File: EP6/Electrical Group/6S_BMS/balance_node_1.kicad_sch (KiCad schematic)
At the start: 8 parts, among them Q4 SI2301CDS-T1-GE3

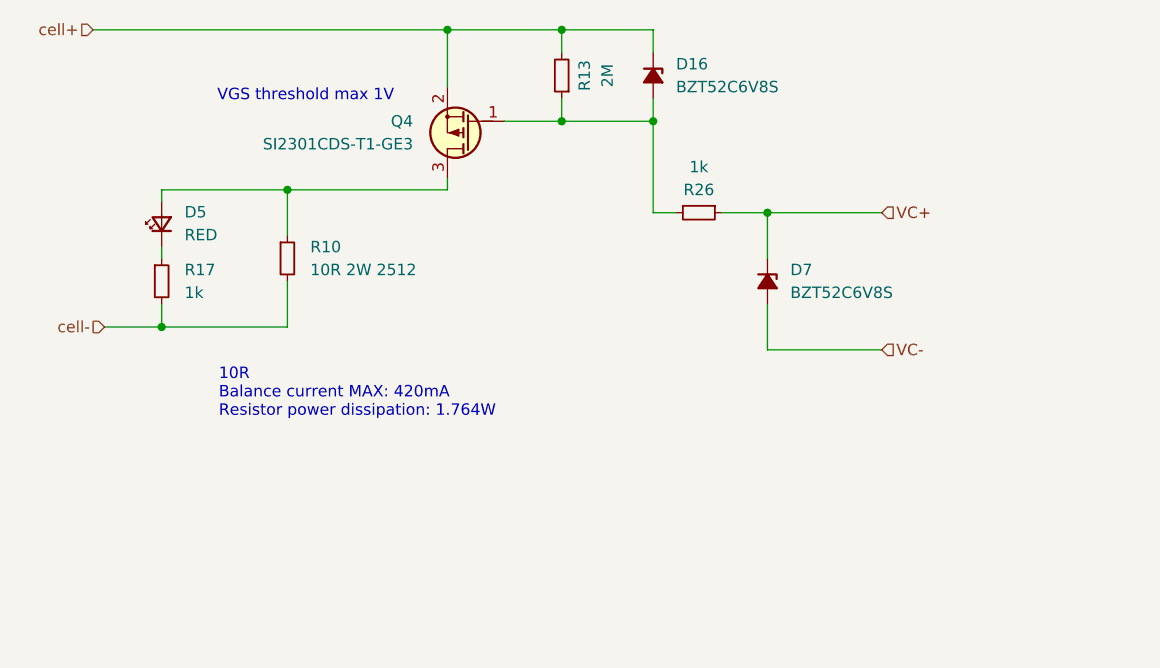
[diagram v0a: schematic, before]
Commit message: 6S BMS sch cleanup
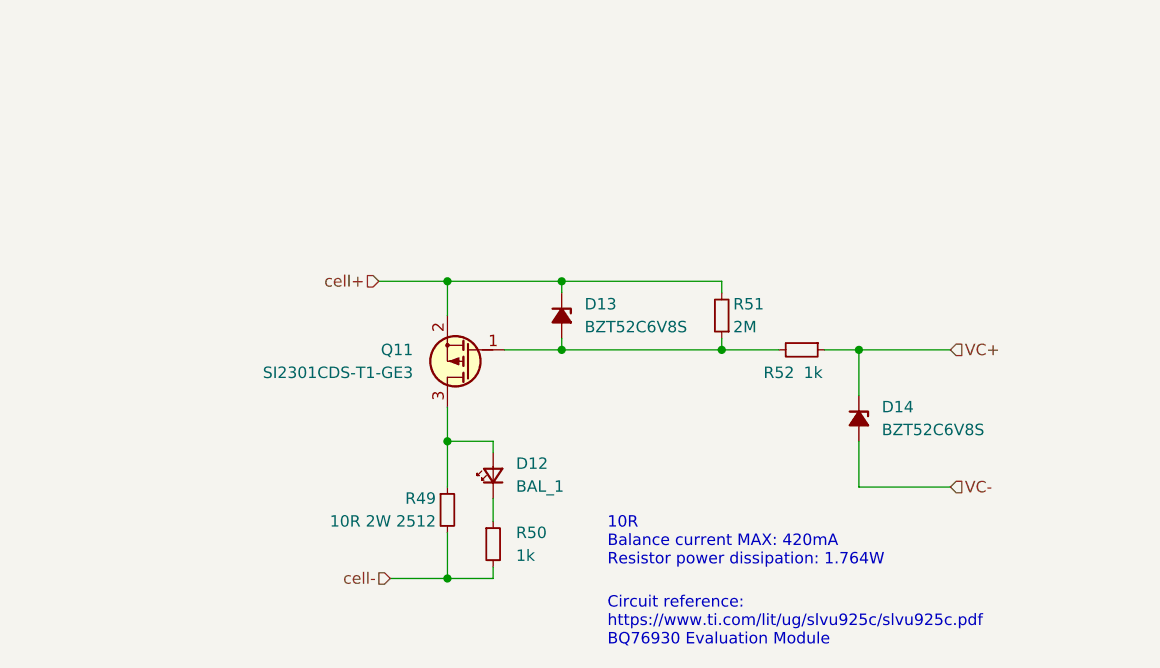
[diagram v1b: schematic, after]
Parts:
- removed D16, D7: BZT52C6V8S, Diode_SMD:D_SOD-323, symbol Device:D_Zener_Small_Filled
- removed D5: RED, LED_SMD:LED_0603_1608Metric, symbol Device:LED_Small
- removed Q4: SI2301CDS-T1-GE3, Package_TO_SOT_SMD:SOT-23, symbol PCM_Transistor_MOSFET_AKL:Q_PMOS-E_Generic_GSD
- removed R10: 10R 2W 2512, Resistor_SMD:R_2512_6332Metric, symbol Device:R_Small
- removed R13: 2M, Resistor_SMD:R_0402_1005Metric, symbol Device:R_Small
- removed R17, R26: 1k, Resistor_SMD:R_0402_1005Metric, symbol Device:R_Small
- added D12: BAL_1, LED_SMD:LED_0603_1608Metric, symbol Device:LED_Small
- added D13, D14: BZT52C6V8S, Diode_SMD:D_SOD-323, symbol Device:D_Zener_Small_Filled
- added Q11: SI2301CDS-T1-GE3, Package_TO_SOT_SMD:SOT-23, symbol PCM_Transistor_MOSFET_AKL:Q_PMOS-E_Generic_GSD
- added R49: 10R 2W 2512, Resistor_SMD:R_2512_6332Metric, symbol Device:R_Small
- added R50, R52: 1k, Resistor_SMD:R_0402_1005Metric, symbol Device:R_Small
- added R51: 2M, Resistor_SMD:R_0402_1005Metric, symbol Device:R_Small
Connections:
- net VC+: now also D14.1 (K), R52.1
- net VC-: now also D14.2 (A)
- net cell+: now also D13.1 (K), Q11.2 (S), R51.2
- net cell-: now also R49.2, R50.2
- new net: D13.2 (A), Q11.1 (G), R51.1, R52.2
- new net: D12.2 (A), Q11.3 (D), R49.1
- new net: D12.1 (K), R50.1
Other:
- note added: "Circuit reference: https://www.ti.com/lit/ug/slvu925c/slvu925c.pdf BQ76930 Evaluation Module"
- note removed: "VGS threshold max 1V"

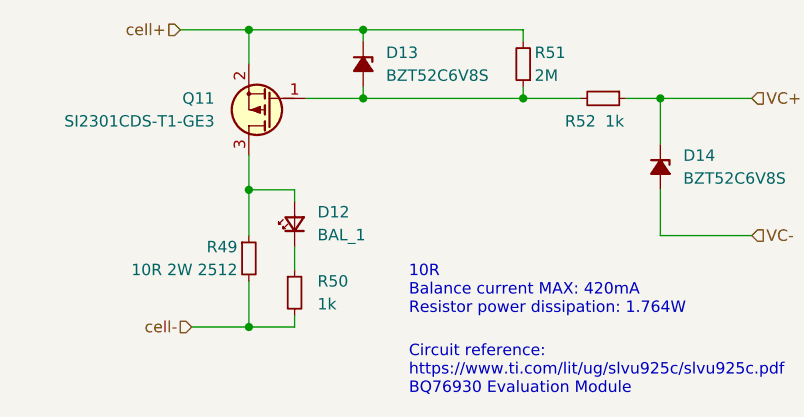
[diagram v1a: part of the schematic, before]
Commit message: fix net ties
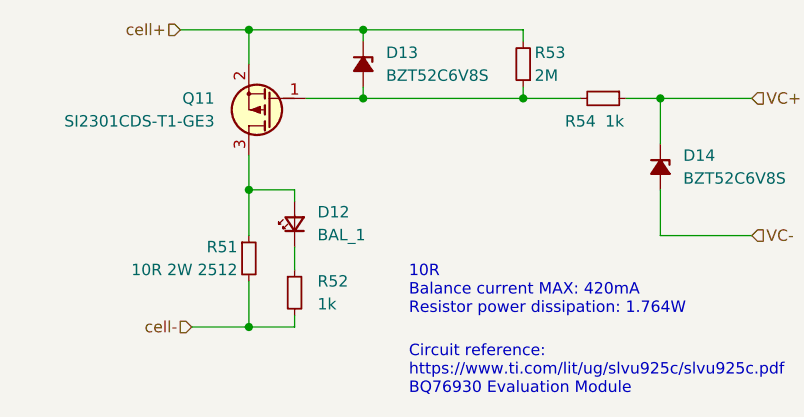
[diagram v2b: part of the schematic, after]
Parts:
- renumbered R49 to R51, R50 to R52, R51 to R53, R52 to R54
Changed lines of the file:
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@@
 		(on_board yes)
 		(dnp no)
-		(property "Reference" "R49"
+		(property "Reference" "R51"
 			(at 127 107.95 0)
 			(effects
@@
 			(project "6S_BMS"
 				(path "/0942010f-46b1-4fe9-9f5e-a3ebd22b3e41/52dfc651-89b8-4cbc-8d60-c4ae9fe4057d"
-					(reference "R49")
-					(unit 1)
-				)
-				(path "/0942010f-46b1-4fe9-9f5e-a3ebd22b3e41/8cdfc8a8-e74f-4198-87ef-7f931d327daa"
-					(reference "R45")
-					(unit 1)
-				)
-				(path "/0942010f-46b1-4fe9-9f5e-a3ebd22b3e41/92fdac40-2976-4651-87ac-086c10e148fd"
-					(reference "R61")
-					(unit 1)
-				)
-				(path "/0942010f-46b1-4fe9-9f5e-a3ebd22b3e41/d0b81097-a7cf-4d08-9411-1236a5f1861b"
-					(reference "R53")
-					(unit 1)
-				)
-				(path "/0942010f-46b1-4fe9-9f5e-a3ebd22b3e41/d47f883f-ac19-4acb-9090-d30d2c19de6d"
-					(reference "R65")
-					(unit 1)
-				)
-				(path "/0942010f-46b1-4fe9-9f5e-a3ebd22b3e41/f57ef34a-2774-492f-8a82-625e3b6c6734"
-					(reference "R57")
+					(reference "R51")
+					(unit 1)
+				)
+				(path "/0942010f-46b1-4fe9-9f5e-a3ebd22b3e41/8cdfc8a8-e74f-4198-87ef-7f931d327daa"
+					(reference "R47")
+					(unit 1)
+				)
+				(path "/0942010f-46b1-4fe9-9f5e-a3ebd22b3e41/92fdac40-2976-4651-87ac-086c10e148fd"
+					(reference "R63")
+					(unit 1)
+				)
+				(path "/0942010f-46b1-4fe9-9f5e-a3ebd22b3e41/d0b81097-a7cf-4d08-9411-1236a5f1861b"
+					(reference "R55")
+					(unit 1)
+				)
+				(path "/0942010f-46b1-4fe9-9f5e-a3ebd22b3e41/d47f883f-ac19-4acb-9090-d30d2c19de6d"
+					(reference "R67")
+					(unit 1)
+				)
+				(path "/0942010f-46b1-4fe9-9f5e-a3ebd22b3e41/f57ef34a-2774-492f-8a82-625e3b6c6734"
+					(reference "R59")
 					(unit 1)
 				)
@@
 		(dnp no)
 		(fields_autoplaced yes)
-		(property "Reference" "R50"
+		(property "Reference" "R52"
 			(at 135.89 111.76 0)
 			(effects
@@
 			(project "6S_BMS"
 				(path "/0942010f-46b1-4fe9-9f5e-a3ebd22b3e41/52dfc651-89b8-4cbc-8d60-c4ae9fe4057d"
-					(reference "R50")
-					(unit 1)
-				)
-				(path "/0942010f-46b1-4fe9-9f5e-a3ebd22b3e41/8cdfc8a8-e74f-4198-87ef-7f931d327daa"
-					(reference "R46")
-					(unit 1)
-				)
-				(path "/0942010f-46b1-4fe9-9f5e-a3ebd22b3e41/92fdac40-2976-4651-87ac-086c10e148fd"
-					(reference "R62")
-					(unit 1)
-				)
-				(path "/0942010f-46b1-4fe9-9f5e-a3ebd22b3e41/d0b81097-a7cf-4d08-9411-1236a5f1861b"
-					(reference "R54")
-					(unit 1)
-				)
-				(path "/0942010f-46b1-4fe9-9f5e-a3ebd22b3e41/d47f883f-ac19-4acb-9090-d30d2c19de6d"
-					(reference "R66")
-					(unit 1)
-				)
-				(path "/0942010f-46b1-4fe9-9f5e-a3ebd22b3e41/f57ef34a-2774-492f-8a82-625e3b6c6734"
-					(reference "R58")
+					(reference "R52")
+					(unit 1)
+				)
+				(path "/0942010f-46b1-4fe9-9f5e-a3ebd22b3e41/8cdfc8a8-e74f-4198-87ef-7f931d327daa"
+					(reference "R48")
+					(unit 1)
+				)
+				(path "/0942010f-46b1-4fe9-9f5e-a3ebd22b3e41/92fdac40-2976-4651-87ac-086c10e148fd"
+					(reference "R64")
+					(unit 1)
+				)
+				(path "/0942010f-46b1-4fe9-9f5e-a3ebd22b3e41/d0b81097-a7cf-4d08-9411-1236a5f1861b"
+					(reference "R56")
+					(unit 1)
+				)
+				(path "/0942010f-46b1-4fe9-9f5e-a3ebd22b3e41/d47f883f-ac19-4acb-9090-d30d2c19de6d"
+					(reference "R68")
+					(unit 1)
+				)
+				(path "/0942010f-46b1-4fe9-9f5e-a3ebd22b3e41/f57ef34a-2774-492f-8a82-625e3b6c6734"
+					(reference "R60")
 					(unit 1)
 				)
@@
 		(on_board yes)
 		(dnp no)
-		(property "Reference" "R51"
+		(property "Reference" "R53"
 			(at 160.02 86.36 0)
 			(effects
@@
 			(project "6S_BMS"
 				(path "/0942010f-46b1-4fe9-9f5e-a3ebd22b3e41/52dfc651-89b8-4cbc-8d60-c4ae9fe4057d"
-					(reference "R51")
-					(unit 1)
-				)
-				(path "/0942010f-46b1-4fe9-9f5e-a3ebd22b3e41/8cdfc8a8-e74f-4198-87ef-7f931d327daa"
-					(reference "R47")
-					(unit 1)
-				)
-				(path "/0942010f-46b1-4fe9-9f5e-a3ebd22b3e41/92fdac40-2976-4651-87ac-086c10e148fd"
-					(reference "R63")
-					(unit 1)
-				)
-				(path "/0942010f-46b1-4fe9-9f5e-a3ebd22b3e41/d0b81097-a7cf-4d08-9411-1236a5f1861b"
-					(reference "R55")
-					(unit 1)
-				)
-				(path "/0942010f-46b1-4fe9-9f5e-a3ebd22b3e41/d47f883f-ac19-4acb-9090-d30d2c19de6d"
-					(reference "R67")
-					(unit 1)
-				)
-				(path "/0942010f-46b1-4fe9-9f5e-a3ebd22b3e41/f57ef34a-2774-492f-8a82-625e3b6c6734"
-					(reference "R59")
+					(reference "R53")
+					(unit 1)
+				)
+				(path "/0942010f-46b1-4fe9-9f5e-a3ebd22b3e41/8cdfc8a8-e74f-4198-87ef-7f931d327daa"
+					(reference "R49")
+					(unit 1)
+				)
+				(path "/0942010f-46b1-4fe9-9f5e-a3ebd22b3e41/92fdac40-2976-4651-87ac-086c10e148fd"
+					(reference "R65")
+					(unit 1)
+				)
+				(path "/0942010f-46b1-4fe9-9f5e-a3ebd22b3e41/d0b81097-a7cf-4d08-9411-1236a5f1861b"
+					(reference "R57")
+					(unit 1)
+				)
+				(path "/0942010f-46b1-4fe9-9f5e-a3ebd22b3e41/d47f883f-ac19-4acb-9090-d30d2c19de6d"
+					(reference "R69")
+					(unit 1)
+				)
+				(path "/0942010f-46b1-4fe9-9f5e-a3ebd22b3e41/f57ef34a-2774-492f-8a82-625e3b6c6734"
+					(reference "R61")
 					(unit 1)
 				)
@@
 		(on_board yes)
 		(dnp no)
-		(property "Reference" "R52"
+		(property "Reference" "R54"
 			(at 165.1 93.98 90)
 			(effects
@@
 			(project "6S_BMS"
 				(path "/0942010f-46b1-4fe9-9f5e-a3ebd22b3e41/52dfc651-89b8-4cbc-8d60-c4ae9fe4057d"
-					(reference "R52")
-					(unit 1)
-				)
-				(path "/0942010f-46b1-4fe9-9f5e-a3ebd22b3e41/8cdfc8a8-e74f-4198-87ef-7f931d327daa"
-					(reference "R48")
-					(unit 1)
-				)
-				(path "/0942010f-46b1-4fe9-9f5e-a3ebd22b3e41/92fdac40-2976-4651-87ac-086c10e148fd"
-					(reference "R64")
-					(unit 1)
-				)
-				(path "/0942010f-46b1-4fe9-9f5e-a3ebd22b3e41/d0b81097-a7cf-4d08-9411-1236a5f1861b"
-					(reference "R56")
-					(unit 1)
-				)
-				(path "/0942010f-46b1-4fe9-9f5e-a3ebd22b3e41/d47f883f-ac19-4acb-9090-d30d2c19de6d"
-					(reference "R68")
-					(unit 1)
-				)
-				(path "/0942010f-46b1-4fe9-9f5e-a3ebd22b3e41/f57ef34a-2774-492f-8a82-625e3b6c6734"
-					(reference "R60")
-					(unit 1)
-				)
+					(reference "R54")
+					(unit 1)
+				)
+				(path "/0942010f-46b1-4fe9-9f5e-a3ebd22b3e41/8cdfc8a8-e74f-4198-87ef-7f931d327daa"
+					(reference "R50")
+					(unit 1)
+				)
+				(path "/0942010f-46b1-4fe9-9f5e-a3ebd22b3e41/92fdac40-2976-4651-87ac-086c10e148fd"
+					(reference "R66")
+					(unit 1)
+				)
+				(path "/0942010f-46b1-4fe9-9f5e-a3ebd22b3e41/d0b81097-a7cf-4d08-9411-1236a5f1861b"
+					(reference "R58")
+					(unit 1)
+				)
+				(path "/0942010f-46b1-4fe9-9f5e-a3ebd22b3e41/d47f883f-ac19-4acb-9090-d30d2c19de6d"
+					(reference "R70")
+					(unit 1)
+				)
+				(path "/0942010f-46b1-4fe9-9f5e-a3ebd22b3e41/f57ef34a-2774-492f-8a82-625e3b6c6734"
+					(reference "R62")
+					(unit 1)
+				)

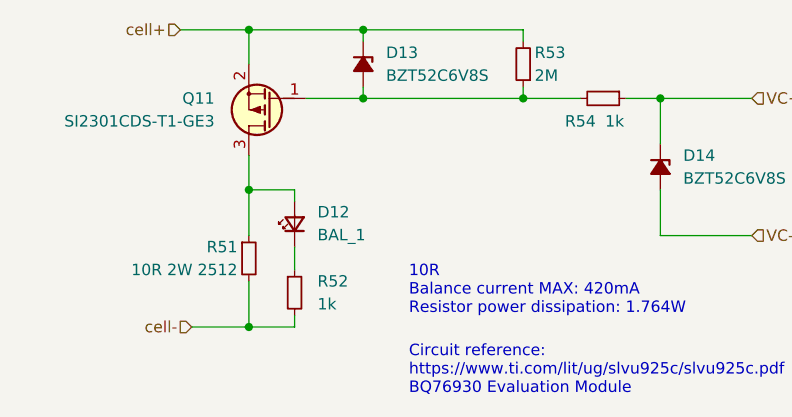
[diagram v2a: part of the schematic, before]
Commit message: front panel board connectors
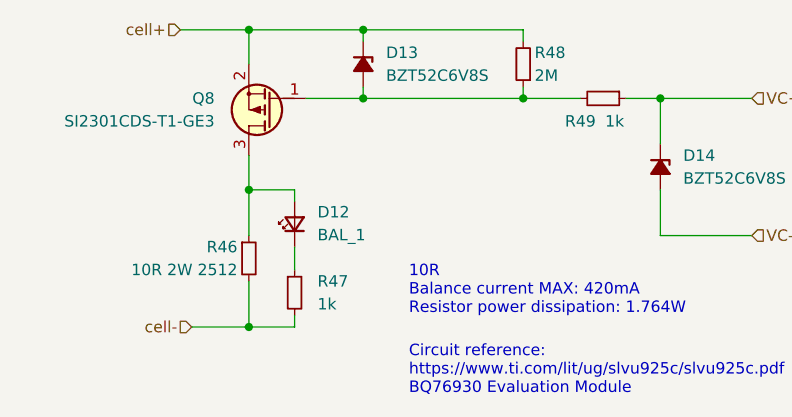
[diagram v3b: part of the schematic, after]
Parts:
- renumbered Q11 to Q8, R51 to R46, R52 to R47, R53 to R48, R54 to R49
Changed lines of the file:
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@@
 		(on_board yes)
 		(dnp no)
-		(property "Reference" "Q11"
+		(property "Reference" "Q8"
 			(at 124.46 91.44 0)
 			(effects
@@
 			(project "6S_BMS"
 				(path "/0942010f-46b1-4fe9-9f5e-a3ebd22b3e41/52dfc651-89b8-4cbc-8d60-c4ae9fe4057d"
+					(reference "Q8")
+					(unit 1)
+				)
+				(path "/0942010f-46b1-4fe9-9f5e-a3ebd22b3e41/8cdfc8a8-e74f-4198-87ef-7f931d327daa"
+					(reference "Q7")
+					(unit 1)
+				)
+				(path "/0942010f-46b1-4fe9-9f5e-a3ebd22b3e41/92fdac40-2976-4651-87ac-086c10e148fd"
 					(reference "Q11")
 					(unit 1)
 				)
-				(path "/0942010f-46b1-4fe9-9f5e-a3ebd22b3e41/8cdfc8a8-e74f-4198-87ef-7f931d327daa"
+				(path "/0942010f-46b1-4fe9-9f5e-a3ebd22b3e41/d0b81097-a7cf-4d08-9411-1236a5f1861b"
+					(reference "Q9")
+					(unit 1)
+				)
+				(path "/0942010f-46b1-4fe9-9f5e-a3ebd22b3e41/d47f883f-ac19-4acb-9090-d30d2c19de6d"
+					(reference "Q12")
+					(unit 1)
+				)
+				(path "/0942010f-46b1-4fe9-9f5e-a3ebd22b3e41/f57ef34a-2774-492f-8a82-625e3b6c6734"
 					(reference "Q10")
-					(unit 1)
-				)
-				(path "/0942010f-46b1-4fe9-9f5e-a3ebd22b3e41/92fdac40-2976-4651-87ac-086c10e148fd"
-					(reference "Q14")
-					(unit 1)
-				)
-				(path "/0942010f-46b1-4fe9-9f5e-a3ebd22b3e41/d0b81097-a7cf-4d08-9411-1236a5f1861b"
-					(reference "Q12")
-					(unit 1)
-				)
-				(path "/0942010f-46b1-4fe9-9f5e-a3ebd22b3e41/d47f883f-ac19-4acb-9090-d30d2c19de6d"
-					(reference "Q15")
-					(unit 1)
-				)
-				(path "/0942010f-46b1-4fe9-9f5e-a3ebd22b3e41/f57ef34a-2774-492f-8a82-625e3b6c6734"
-					(reference "Q13")
 					(unit 1)
 				)
@@
 		(on_board yes)
 		(dnp no)
-		(property "Reference" "R51"
+		(property "Reference" "R46"
 			(at 127 107.95 0)
 			(effects
@@
 			(project "6S_BMS"
 				(path "/0942010f-46b1-4fe9-9f5e-a3ebd22b3e41/52dfc651-89b8-4cbc-8d60-c4ae9fe4057d"
-					(reference "R51")
-					(unit 1)
-				)
-				(path "/0942010f-46b1-4fe9-9f5e-a3ebd22b3e41/8cdfc8a8-e74f-4198-87ef-7f931d327daa"
-					(reference "R47")
-					(unit 1)
-				)
-				(path "/0942010f-46b1-4fe9-9f5e-a3ebd22b3e41/92fdac40-2976-4651-87ac-086c10e148fd"
-					(reference "R63")
-					(unit 1)
-				)
-				(path "/0942010f-46b1-4fe9-9f5e-a3ebd22b3e41/d0b81097-a7cf-4d08-9411-1236a5f1861b"
-					(reference "R55")
-					(unit 1)
-				)
-				(path "/0942010f-46b1-4fe9-9f5e-a3ebd22b3e41/d47f883f-ac19-4acb-9090-d30d2c19de6d"
-					(reference "R67")
-					(unit 1)
-				)
-				(path "/0942010f-46b1-4fe9-9f5e-a3ebd22b3e41/f57ef34a-2774-492f-8a82-625e3b6c6734"
-					(reference "R59")
+					(reference "R46")
+					(unit 1)
+				)
+				(path "/0942010f-46b1-4fe9-9f5e-a3ebd22b3e41/8cdfc8a8-e74f-4198-87ef-7f931d327daa"
+					(reference "R42")
+					(unit 1)
+				)
+				(path "/0942010f-46b1-4fe9-9f5e-a3ebd22b3e41/92fdac40-2976-4651-87ac-086c10e148fd"
+					(reference "R58")
+					(unit 1)
+				)
+				(path "/0942010f-46b1-4fe9-9f5e-a3ebd22b3e41/d0b81097-a7cf-4d08-9411-1236a5f1861b"
+					(reference "R50")
+					(unit 1)
+				)
+				(path "/0942010f-46b1-4fe9-9f5e-a3ebd22b3e41/d47f883f-ac19-4acb-9090-d30d2c19de6d"
+					(reference "R62")
+					(unit 1)
+				)
+				(path "/0942010f-46b1-4fe9-9f5e-a3ebd22b3e41/f57ef34a-2774-492f-8a82-625e3b6c6734"
+					(reference "R54")
 					(unit 1)
 				)
@@
 		(dnp no)
 		(fields_autoplaced yes)
-		(property "Reference" "R52"
+		(property "Reference" "R47"
 			(at 135.89 111.76 0)
 			(effects
@@
 			(project "6S_BMS"
 				(path "/0942010f-46b1-4fe9-9f5e-a3ebd22b3e41/52dfc651-89b8-4cbc-8d60-c4ae9fe4057d"
-					(reference "R52")
-					(unit 1)
-				)
-				(path "/0942010f-46b1-4fe9-9f5e-a3ebd22b3e41/8cdfc8a8-e74f-4198-87ef-7f931d327daa"
-					(reference "R48")
-					(unit 1)
-				)
-				(path "/0942010f-46b1-4fe9-9f5e-a3ebd22b3e41/92fdac40-2976-4651-87ac-086c10e148fd"
-					(reference "R64")
-					(unit 1)
-				)
-				(path "/0942010f-46b1-4fe9-9f5e-a3ebd22b3e41/d0b81097-a7cf-4d08-9411-1236a5f1861b"
-					(reference "R56")
-					(unit 1)
-				)
-				(path "/0942010f-46b1-4fe9-9f5e-a3ebd22b3e41/d47f883f-ac19-4acb-9090-d30d2c19de6d"
-					(reference "R68")
-					(unit 1)
-				)
-				(path "/0942010f-46b1-4fe9-9f5e-a3ebd22b3e41/f57ef34a-2774-492f-8a82-625e3b6c6734"
-					(reference "R60")
+					(reference "R47")
+					(unit 1)
+				)
+				(path "/0942010f-46b1-4fe9-9f5e-a3ebd22b3e41/8cdfc8a8-e74f-4198-87ef-7f931d327daa"
+					(reference "R43")
+					(unit 1)
+				)
+				(path "/0942010f-46b1-4fe9-9f5e-a3ebd22b3e41/92fdac40-2976-4651-87ac-086c10e148fd"
+					(reference "R59")
+					(unit 1)
+				)
+				(path "/0942010f-46b1-4fe9-9f5e-a3ebd22b3e41/d0b81097-a7cf-4d08-9411-1236a5f1861b"
+					(reference "R51")
+					(unit 1)
+				)
+				(path "/0942010f-46b1-4fe9-9f5e-a3ebd22b3e41/d47f883f-ac19-4acb-9090-d30d2c19de6d"
+					(reference "R63")
+					(unit 1)
+				)
+				(path "/0942010f-46b1-4fe9-9f5e-a3ebd22b3e41/f57ef34a-2774-492f-8a82-625e3b6c6734"
+					(reference "R55")
 					(unit 1)
 				)
@@
 		(on_board yes)
 		(dnp no)
-		(property "Reference" "R53"
+		(property "Reference" "R48"
 			(at 160.02 86.36 0)
 			(effects
@@
 			(project "6S_BMS"
 				(path "/0942010f-46b1-4fe9-9f5e-a3ebd22b3e41/52dfc651-89b8-4cbc-8d60-c4ae9fe4057d"
-					(reference "R53")
-					(unit 1)
-				)
-				(path "/0942010f-46b1-4fe9-9f5e-a3ebd22b3e41/8cdfc8a8-e74f-4198-87ef-7f931d327daa"
-					(reference "R49")
-					(unit 1)
-				)
-				(path "/0942010f-46b1-4fe9-9f5e-a3ebd22b3e41/92fdac40-2976-4651-87ac-086c10e148fd"
-					(reference "R65")
-					(unit 1)
-				)
-				(path "/0942010f-46b1-4fe9-9f5e-a3ebd22b3e41/d0b81097-a7cf-4d08-9411-1236a5f1861b"
-					(reference "R57")
-					(unit 1)
-				)
-				(path "/0942010f-46b1-4fe9-9f5e-a3ebd22b3e41/d47f883f-ac19-4acb-9090-d30d2c19de6d"
-					(reference "R69")
-					(unit 1)
-				)
-				(path "/0942010f-46b1-4fe9-9f5e-a3ebd22b3e41/f57ef34a-2774-492f-8a82-625e3b6c6734"
-					(reference "R61")
+					(reference "R48")
+					(unit 1)
+				)
+				(path "/0942010f-46b1-4fe9-9f5e-a3ebd22b3e41/8cdfc8a8-e74f-4198-87ef-7f931d327daa"
+					(reference "R44")
+					(unit 1)
+				)
+				(path "/0942010f-46b1-4fe9-9f5e-a3ebd22b3e41/92fdac40-2976-4651-87ac-086c10e148fd"
+					(reference "R60")
+					(unit 1)
+				)
+				(path "/0942010f-46b1-4fe9-9f5e-a3ebd22b3e41/d0b81097-a7cf-4d08-9411-1236a5f1861b"
+					(reference "R52")
+					(unit 1)
+				)
+				(path "/0942010f-46b1-4fe9-9f5e-a3ebd22b3e41/d47f883f-ac19-4acb-9090-d30d2c19de6d"
+					(reference "R64")
+					(unit 1)
+				)
+				(path "/0942010f-46b1-4fe9-9f5e-a3ebd22b3e41/f57ef34a-2774-492f-8a82-625e3b6c6734"
+					(reference "R56")
 					(unit 1)
 				)
@@
 		(on_board yes)
 		(dnp no)
-		(property "Reference" "R54"
+		(property "Reference" "R49"
 			(at 165.1 93.98 90)
 			(effects
@@
 			(project "6S_BMS"
 				(path "/0942010f-46b1-4fe9-9f5e-a3ebd22b3e41/52dfc651-89b8-4cbc-8d60-c4ae9fe4057d"
-					(reference "R54")
-					(unit 1)
-				)
-				(path "/0942010f-46b1-4fe9-9f5e-a3ebd22b3e41/8cdfc8a8-e74f-4198-87ef-7f931d327daa"
-					(reference "R50")
-					(unit 1)
-				)
-				(path "/0942010f-46b1-4fe9-9f5e-a3ebd22b3e41/92fdac40-2976-4651-87ac-086c10e148fd"
-					(reference "R66")
-					(unit 1)
-				)
-				(path "/0942010f-46b1-4fe9-9f5e-a3ebd22b3e41/d0b81097-a7cf-4d08-9411-1236a5f1861b"
-					(reference "R58")
-					(unit 1)
-				)
-				(path "/0942010f-46b1-4fe9-9f5e-a3ebd22b3e41/d47f883f-ac19-4acb-9090-d30d2c19de6d"
-					(reference "R70")
-					(unit 1)
-				)
-				(path "/0942010f-46b1-4fe9-9f5e-a3ebd22b3e41/f57ef34a-2774-492f-8a82-625e3b6c6734"
-					(reference "R62")
-					(unit 1)
-				)
+					(reference "R49")
+					(unit 1)
+				)
+				(path "/0942010f-46b1-4fe9-9f5e-a3ebd22b3e41/8cdfc8a8-e74f-4198-87ef-7f931d327daa"
+					(reference "R45")
+					(unit 1)
+				)
+				(path "/0942010f-46b1-4fe9-9f5e-a3ebd22b3e41/92fdac40-2976-4651-87ac-086c10e148fd"
+					(reference "R61")
+					(unit 1)
+				)
+				(path "/0942010f-46b1-4fe9-9f5e-a3ebd22b3e41/d0b81097-a7cf-4d08-9411-1236a5f1861b"
+					(reference "R53")
+					(unit 1)
+				)
+				(path "/0942010f-46b1-4fe9-9f5e-a3ebd22b3e41/d47f883f-ac19-4acb-9090-d30d2c19de6d"
+					(reference "R65")
+					(unit 1)
+				)
+				(path "/0942010f-46b1-4fe9-9f5e-a3ebd22b3e41/f57ef34a-2774-492f-8a82-625e3b6c6734"
+					(reference "R57")
+					(unit 1)
+				)
